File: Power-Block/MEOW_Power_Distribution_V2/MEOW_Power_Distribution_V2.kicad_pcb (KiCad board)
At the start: 2 copper layers, 75 x 49 mm, 19 parts, among them J3 Terminal Out (Screw), J4 Terminal Out (Screw), J6 Terminal Out (Screw), U1 3.3V LM2596S-3.3 LM2596S-3.3, U2 5V LM2596S-5 LM2596S-5

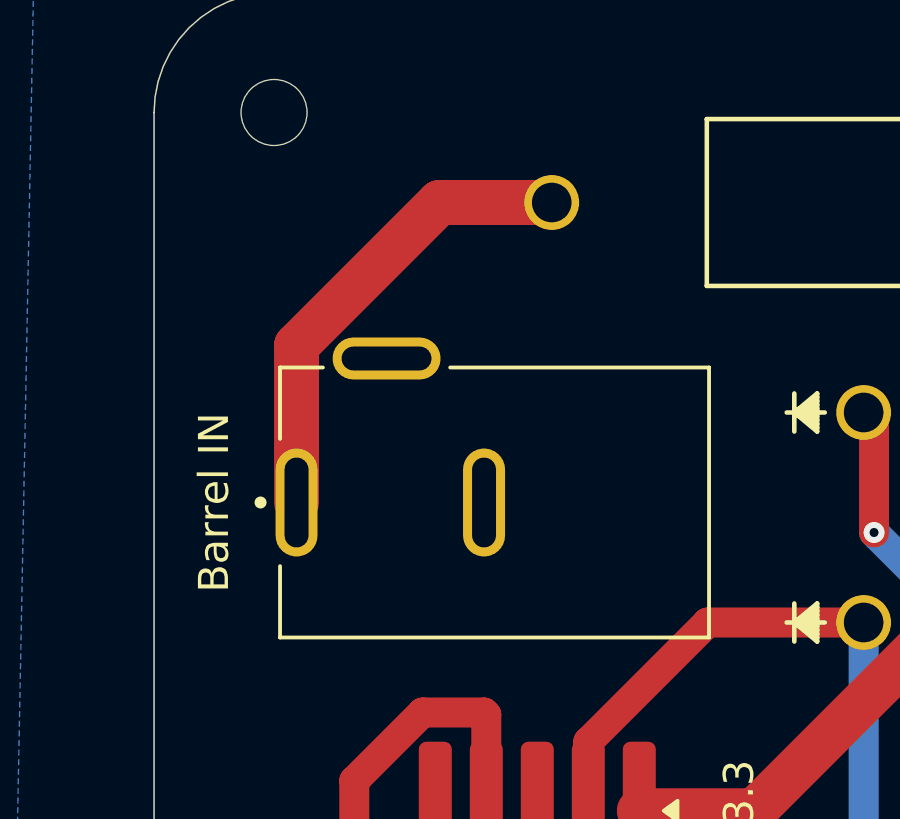
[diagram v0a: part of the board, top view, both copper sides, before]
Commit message: Added A system intergration schematic
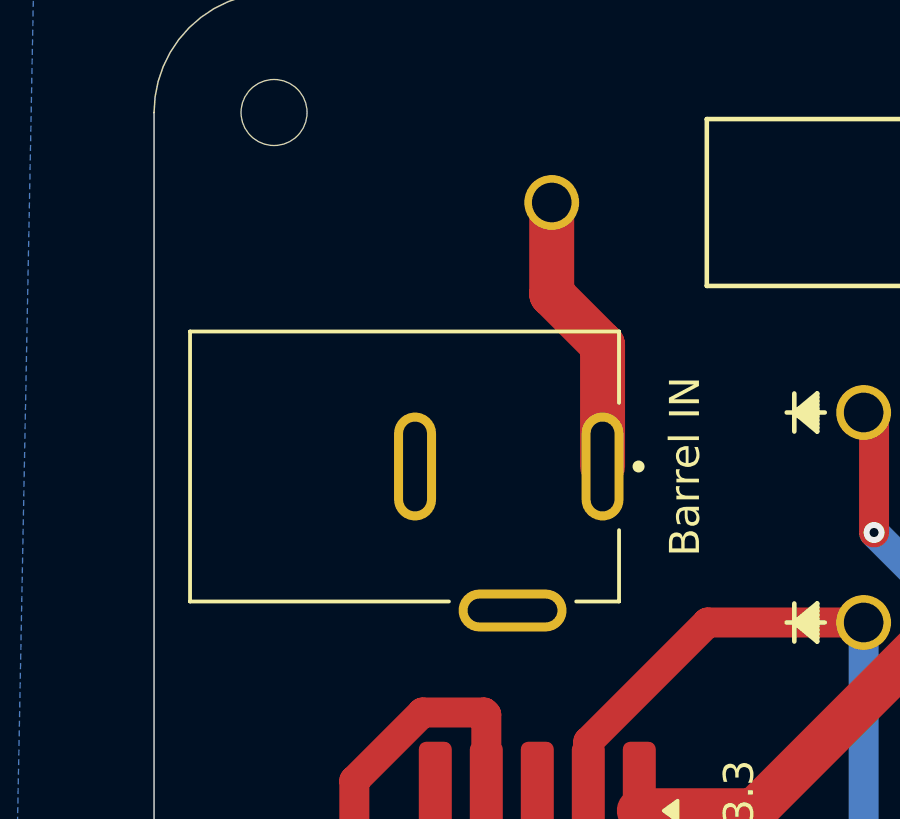
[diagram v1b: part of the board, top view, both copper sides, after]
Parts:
- moved Barrel IN 2.59 mm to (29.7, 31.8), turned to -90 degrees
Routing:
- net Net-(D2-A): track 15.7 -> 9.50 mm
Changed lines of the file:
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@@
 	(footprint "footprints:TENSILITY_54-00166"
 		(layer "F.Cu")
-		(at 32 33 90)
+		(at 29.7 31.8 -90)
 		(property "Reference" "Barrel IN"
-			(at 0 -9 -90)
+			(at 0 -9 90)
 			(layer "F.SilkS")
 			(effects
@@
 		)
 		(property "Value" "54-00166"
-			(at -3 2 180)
+			(at -3 2 0)
 			(layer "F.Fab")
 			(effects
@@
 		)
 		(property "PARTREV" "A"
-			(at 0 0 90)
+			(at 0 0 -90)
 			(unlocked yes)
 			(layer "F.Fab")
@@
 		)
 		(property "STANDARD" "Manufacturer Recommendations"
-			(at 0 0 90)
+			(at 0 0 -90)
 			(unlocked yes)
 			(layer "F.Fab")
@@
 		)
 		(property "SNAPEDA_PN" "54-00166"
-			(at 0 0 90)
+			(at 0 0 -90)
 			(unlocked yes)
 			(layer "F.Fab")
@@
 		)
 		(property "MAXIMUM_PACKAGE_HEIGHT" "11.2mm"
-			(at 0 0 90)
+			(at 0 0 -90)
 			(unlocked yes)
 			(layer "F.Fab")
@@
 		)
 		(property "MANUFACTURER" "TENSILITY"
-			(at 0 0 90)
+			(at 0 0 -90)
 			(unlocked yes)
 			(layer "F.Fab")
@@
 		(attr through_hole)
 		(fp_line
-			(start 4.5 -6.8)
-			(end 4.5 -5.37)
+			(start -4.5 7.5)
+			(end -4.5 -6.8)
 			(stroke
 				(width 0.127)
@@
 		)
 		(fp_line
-			(start 2.12 -6.8)
-			(end 4.5 -6.8)
+			(start 4.5 7.5)
+			(end -4.5 7.5)
 			(stroke
 				(width 0.127)
@@
 		)
 		(fp_line
-			(start -4.5 -6.8)
-			(end -2.12 -6.8)
+			(start 4.5 7.5)
+			(end 4.5 -1.13)
 			(stroke
 				(width 0.127)
@@
 		)
 		(fp_line
-			(start 4.5 7.5)
-			(end 4.5 -1.13)
+			(start -4.5 -6.8)
+			(end -2.12 -6.8)
 			(stroke
 				(width 0.127)
@@
 		)
 		(fp_line
-			(start 4.5 7.5)
-			(end -4.5 7.5)
+			(start 2.12 -6.8)
+			(end 4.5 -6.8)
 			(stroke
 				(width 0.127)
@@
 		)
 		(fp_line
-			(start -4.5 7.5)
-			(end -4.5 -6.8)
+			(start 4.5 -6.8)
+			(end 4.5 -5.37)
 			(stroke
 				(width 0.127)
@@
 		)
 		(fp_line
-			(start 5.75 -7.2)
-			(end -4.75 -7.2)
+			(start -4.75 7.75)
+			(end 5.75 7.75)
 			(stroke
 				(width 0.05)
@@
 		)
 		(fp_line
-			(start -4.75 -7.2)
-			(end -4.75 7.75)
+			(start 5.75 7.75)
+			(end 5.75 -7.2)
 			(stroke
 				(width 0.05)
@@
 		)
 		(fp_line
-			(start 5.75 7.75)
-			(end 5.75 -7.2)
+			(start -4.75 -7.2)
+			(end -4.75 7.75)
 			(stroke
 				(width 0.05)
@@
 		)
 		(fp_line
-			(start -4.75 7.75)
-			(end 5.75 7.75)
+			(start 5.75 -7.2)
+			(end -4.75 -7.2)
 			(stroke
 				(width 0.05)
@@
 		)
 		(fp_line
-			(start 4.5 -6.8)
-			(end 4.5 7.5)
+			(start -4.5 7.5)
+			(end -4.5 -6.8)
 			(stroke
 				(width 0.127)
@@
 		)
 		(fp_line
-			(start -4.5 -6.8)
-			(end 4.5 -6.8)
+			(start 4.5 7.5)
+			(end -4.5 7.5)
 			(stroke
 				(width 0.127)
@@
 		)
 		(fp_line
-			(start 4.5 7.5)
-			(end -4.5 7.5)
+			(start -4.5 -6.8)
+			(end 4.5 -6.8)
 			(stroke
 				(width 0.127)
@@
 		)
 		(fp_line
-			(start -4.5 7.5)
-			(end -4.5 -6.8)
+			(start 4.5 -6.8)
+			(end 4.5 7.5)
 			(stroke
 				(width 0.127)
@@
 		)
 		(pad "A" thru_hole oval
-			(at 0 -6.25 90)
+			(at 0 -6.25 270)
 			(size 3.6 1.4)
 			(drill oval 3 0.8)
@@
 		)
 		(pad "B" thru_hole oval
-			(at 0 0 90)
+			(at 0 0 270)
 			(size 3.6 1.4)
 			(drill oval 3 0.8)
@@
 		)
 		(pad "C" thru_hole oval
-			(at 4.8 -3.25 90)
+			(at 4.8 -3.25 270)
 			(size 1.4 3.6)
 			(drill oval 0.8 3)
@@
 	)
 	(segment
-		(start 25.75 27.766548)
-		(end 25.75 33)
+		(start 34.2558 23)
+		(end 34.2558 26.0558)
 		(width 1.5)
 		(layer "F.Cu")
@@
 	)
 	(segment
-		(start 34.2558 23)
-		(end 30.516548 23)
+		(start 35.95 27.75)
+		(end 35.95 31.8)
 		(width 1.5)
 		(layer "F.Cu")
@@
 	)
 	(segment
-		(start 30.516548 23)
-		(end 25.75 27.766548)
+		(start 34.2558 26.0558)
+		(end 35.95 27.75)
 		(width 1.5)
 		(layer "F.Cu")
